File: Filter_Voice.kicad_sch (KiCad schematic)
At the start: 26 parts, among them U3 TL074, U5 SSI2144

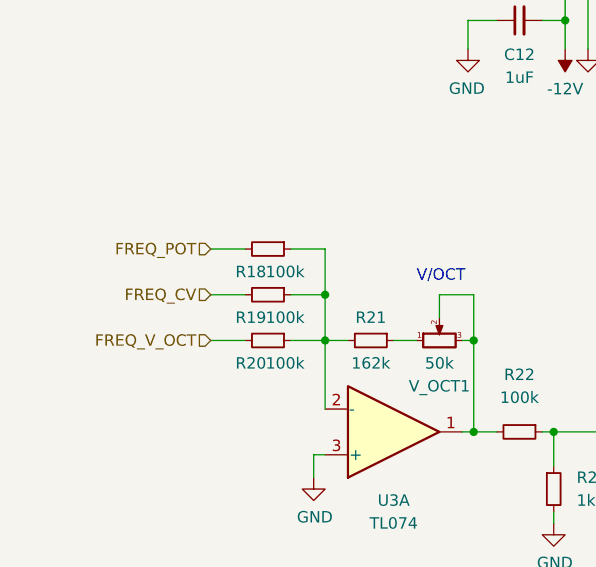
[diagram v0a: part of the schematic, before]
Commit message: Added all voice filter CV; panel draft done
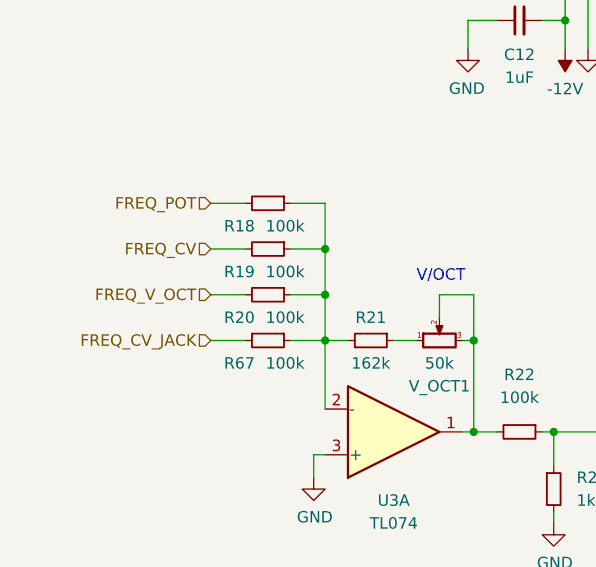
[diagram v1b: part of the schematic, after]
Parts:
- added R67: 100k, Resistor_SMD:R_0603_1608Metric_Pad0.98x0.95mm_HandSolder, symbol Device:R_Small
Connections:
- net at R18.1, R19.1, R20.1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: now also R67.1
- new net FREQ_CV_JACK: R67.2
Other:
- moved on the sheet: R18, R19, R20

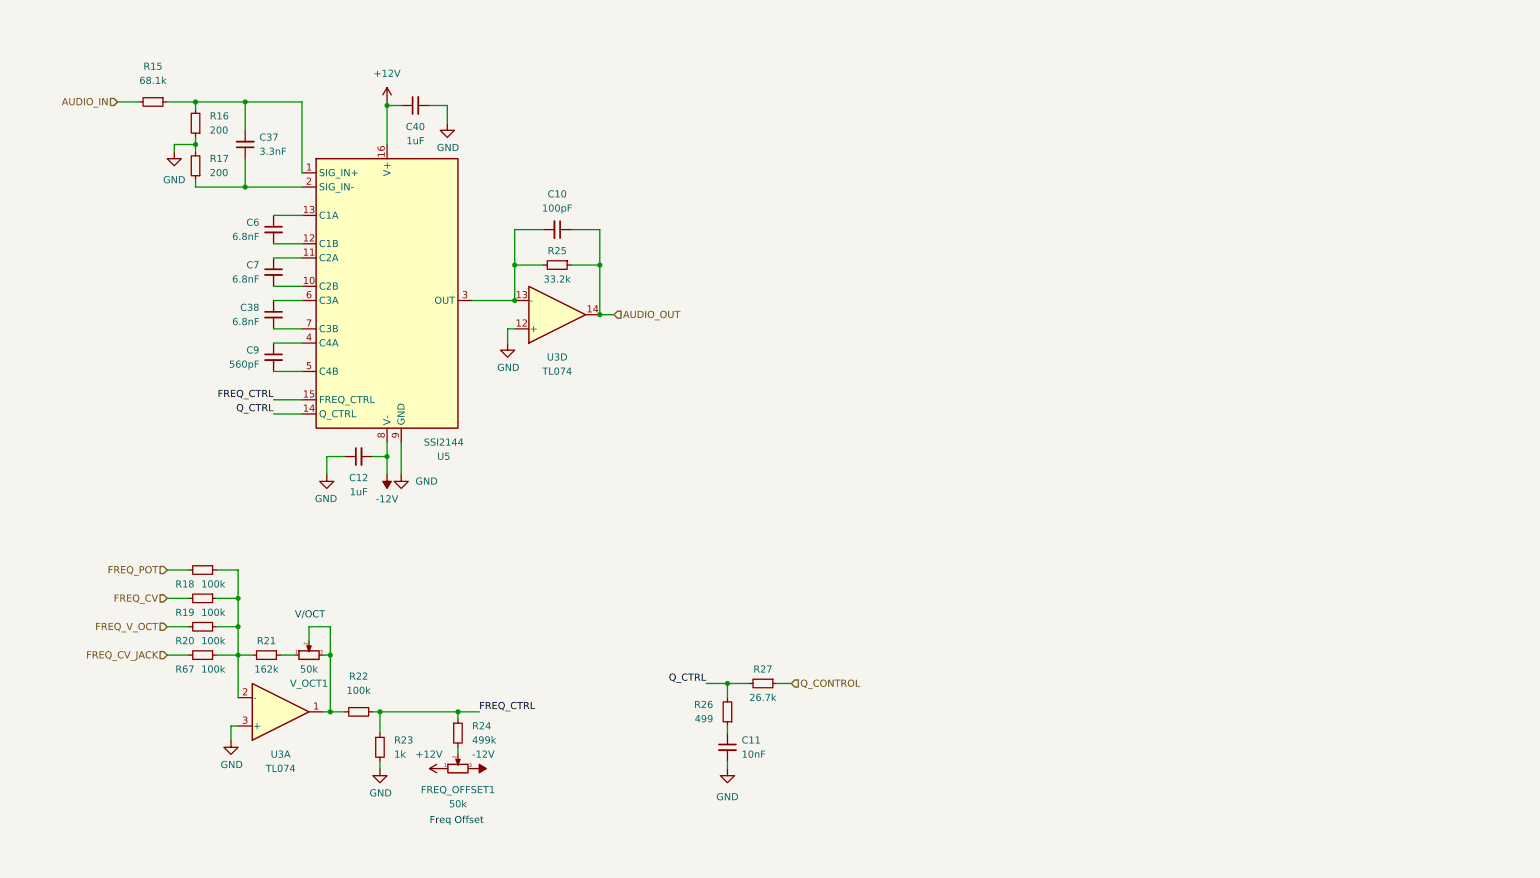
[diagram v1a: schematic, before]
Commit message: Schematic formatting
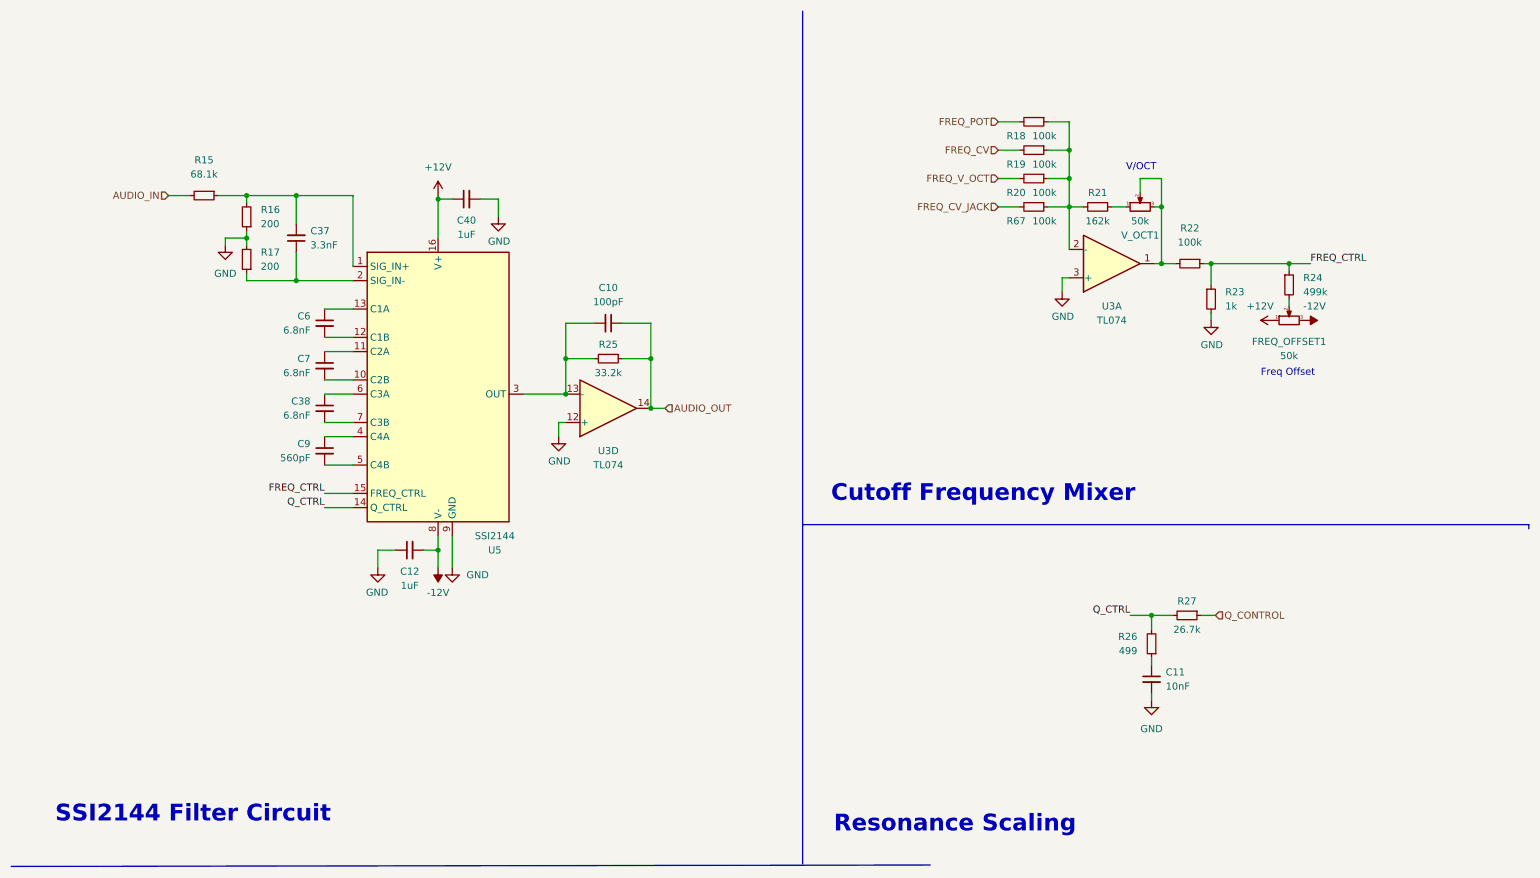
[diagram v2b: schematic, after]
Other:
- note added: "Cutoff Frequency Mixer"
- note added: "Resonance Scaling"
- note added: "SSI2144 Filter Circuit"
- moved on the sheet: C10, C11, C12, C37, C38, C40, C6, C7, C9, FREQ_OFFSET1, R15, R16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

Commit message: Cleaned up panel and PCBs
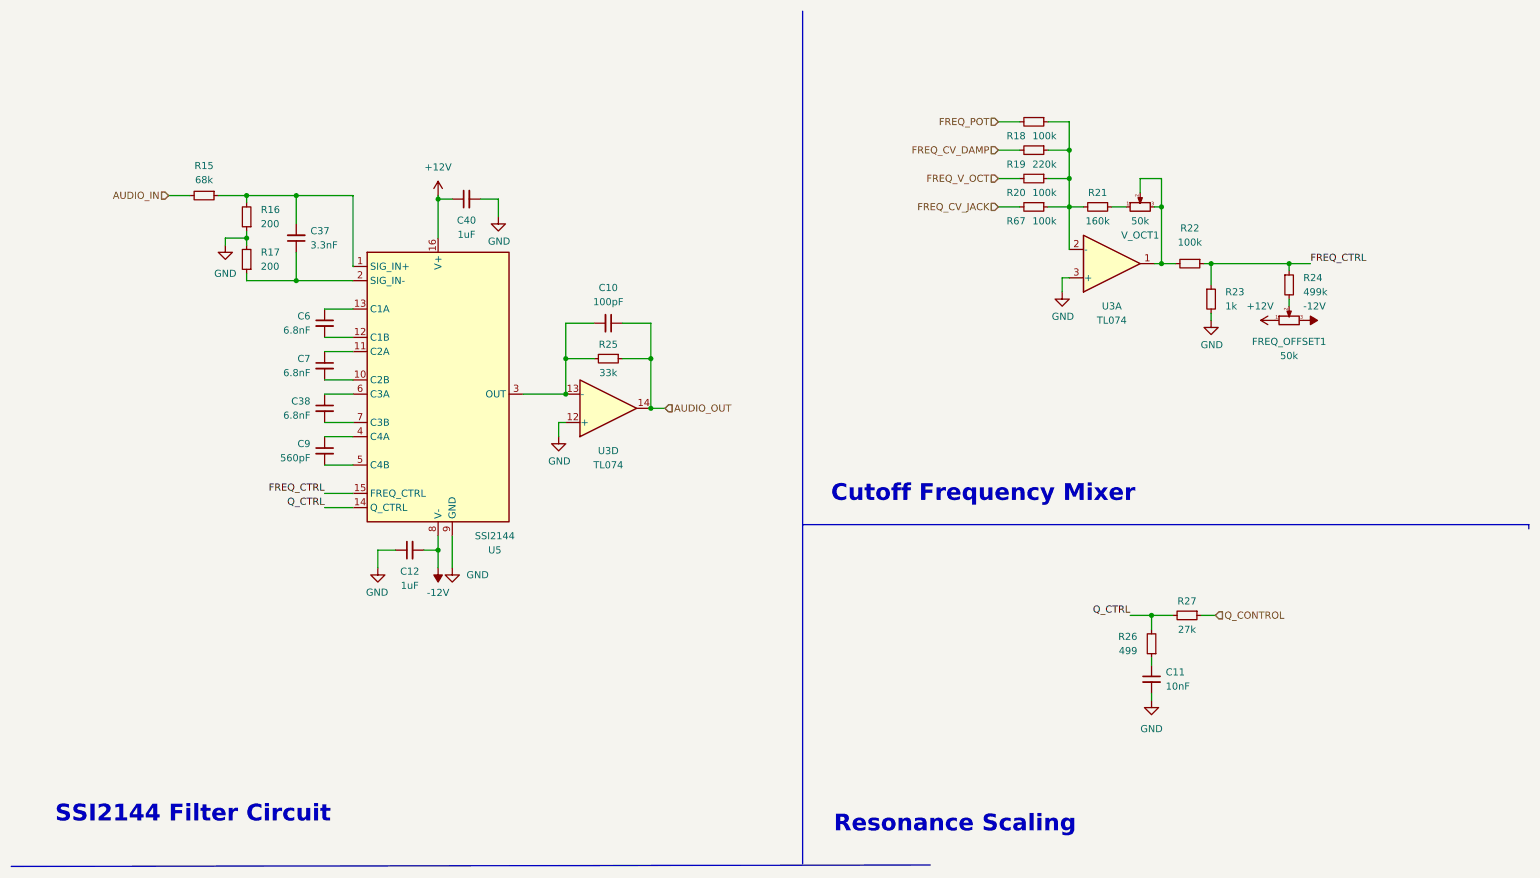
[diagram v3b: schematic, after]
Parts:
- R15: value 68.1k -> 68k
- R19: value 100k -> 220k
- R21: value 162k -> 160k
- R25: value 33.2k -> 33k
- R27: value 26.7k -> 27k
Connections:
- net FREQ_CV renamed FREQ_CV_DAMP
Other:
- note removed: "Freq Offset"
- note removed: "V/OCT"
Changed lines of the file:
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@@
     (effects (font (size 3 3) (thickness 0.6) bold) (justify left bottom))
-  )
-  (text "V/OCT" (at 212.344 41.656 0)
-    (effects (font (size 1.27 1.27)) (justify left bottom))
   )
   (text "SSI2144 Filter Circuit" (at 20.574 158.496 0)
     (effects (font (size 3 3) (thickness 0.6) bold) (justify left bottom))
   )
-  (text "Freq Offset" (at 236.474 78.486 0)
-    (effects (font (size 1.27 1.27)) (justify left bottom))
-  )
   (text "Resonance Scaling" (at 160.02 160.274 0)
     (effects (font (size 3 3) (thickness 0.6) bold) (justify left bottom))
@@
     (effects (font (size 1.27 1.27)) (justify right bottom))
   )
-  (hierarchical_label "FREQ_CV" (shape input) (at 189.484 37.846 180)
+  (hierarchical_label "FREQ_CV_DAMP" (shape input) (at 189.484 37.846 180)
     (effects (font (size 1.27 1.27)) (justify right))
   )
@@
   (symbol (lib_id "Device:R_Small") (at 47.244 45.974 270) (unit 1)
     (in_bom yes) (on_board yes) (fields_autoplaced)
-    (property "Reference" "R15" (id 0) (at 47.244 39.624 90))
-    (property "Value" "68.1k" (id 1) (at 47.244 42.164 90))
+    (property "Reference" "R15" (id 0) (at 47.244 40.64 90))
+    (property "Value" "68k" (id 1) (at 47.244 43.18 90))
     (property "Footprint" "Resistor_SMD:R_0603_1608Metric_Pad0.98x0.95mm_HandSolder" (id 2) (at 47.244 45.974 0)
       (effects (font (size 1.27 1.27)) hide)
@@
     (in_bom yes) (on_board yes)
     (property "Reference" "R21" (id 0) (at 207.264 45.466 90))
-    (property "Value" "162k" (id 1) (at 207.264 50.546 90))
+    (property "Value" "160k" (id 1) (at 207.264 50.546 90))
     (property "Footprint" "Resistor_SMD:R_0603_1608Metric_Pad0.98x0.95mm_HandSolder" (id 2) (at 207.264 48.006 0)
       (effects (font (size 1.27 1.27)) hide)
@@
     (in_bom yes) (on_board yes)
     (property "Reference" "R25" (id 0) (at 119.634 72.644 90))
-    (property "Value" "33.2k" (id 1) (at 119.634 77.724 90))
+    (property "Value" "33k" (id 1) (at 119.634 77.724 90))
     (property "Footprint" "Resistor_SMD:R_0603_1608Metric_Pad0.98x0.95mm_HandSolder" (id 2) (at 119.634 75.184 0)
       (effects (font (size 1.27 1.27)) hide)
@@
     (in_bom yes) (on_board yes)
     (property "Reference" "R27" (id 0) (at 223.266 118.618 90))
-    (property "Value" "26.7k" (id 1) (at 223.266 123.698 90))
+    (property "Value" "27k" (id 1) (at 223.266 123.698 90))
     (property "Footprint" "Resistor_SMD:R_0603_1608Metric_Pad0.98x0.95mm_HandSolder" (id 2) (at 223.266 121.158 0)
       (effects (font (size 1.27 1.27)) hide)
@@
     (in_bom yes) (on_board yes)
     (property "Reference" "R19" (id 0) (at 192.659 40.386 90))
-    (property "Value" "100k" (id 1) (at 197.739 40.386 90))
+    (property "Value" "220k" (id 1) (at 197.739 40.386 90))
     (property "Footprint" "Resistor_SMD:R_0603_1608Metric_Pad0.98x0.95mm_HandSolder" (id 2) (at 195.834 37.846 0)
       (effects (font (size 1.27 1.27)) hide)

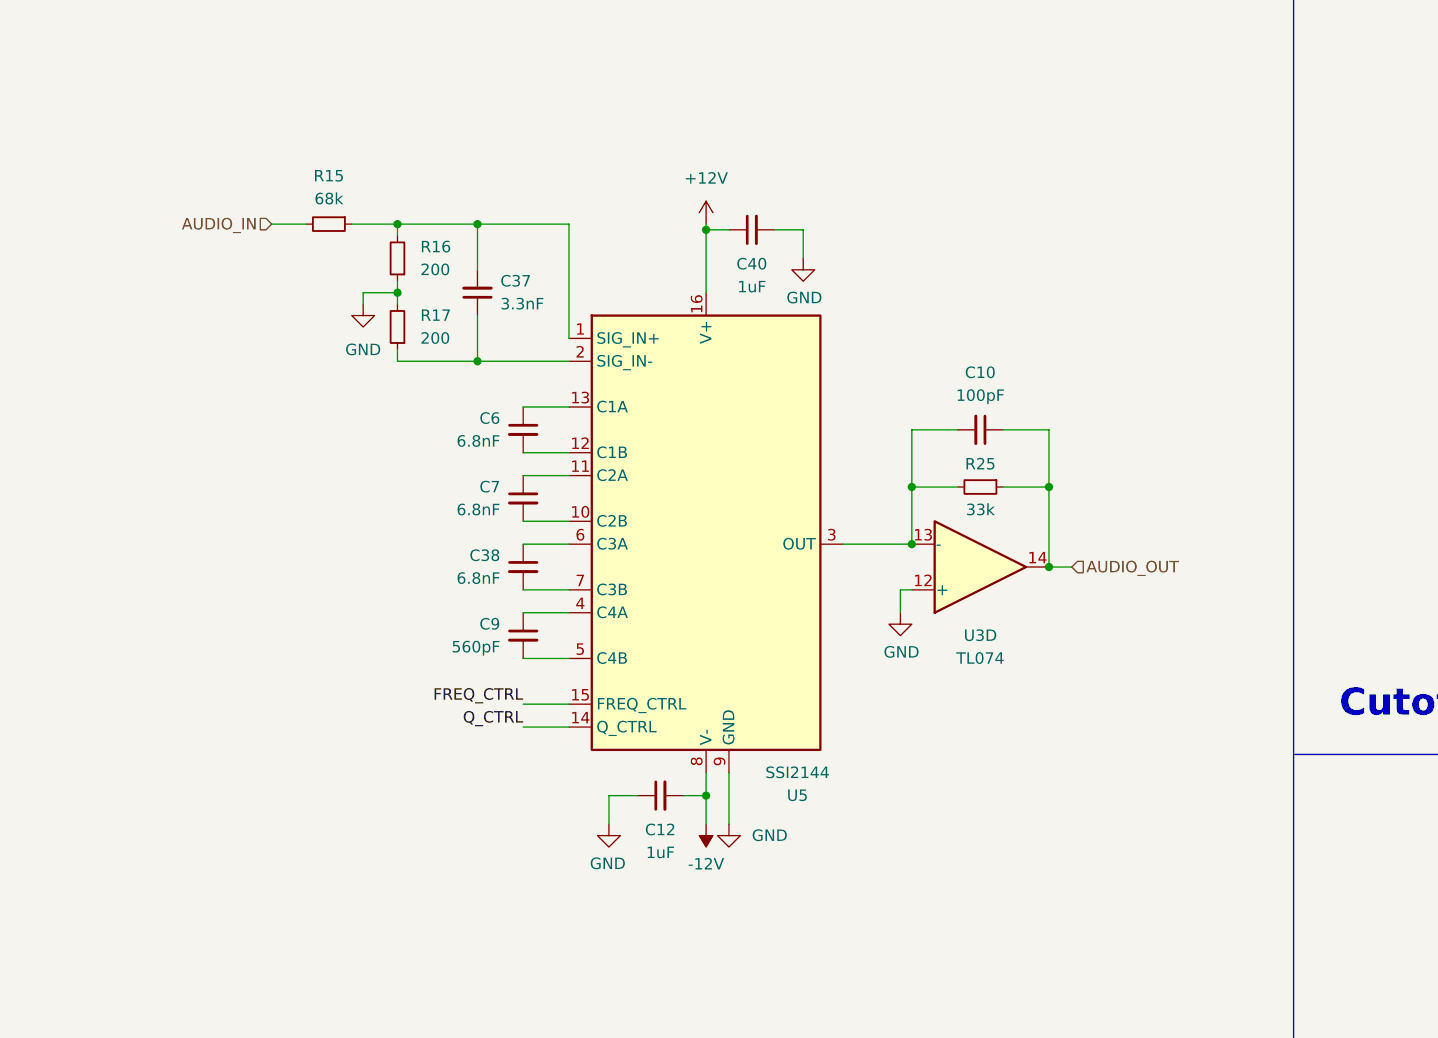
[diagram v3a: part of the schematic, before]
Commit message: Started adding DC blocking caps to audio outputs
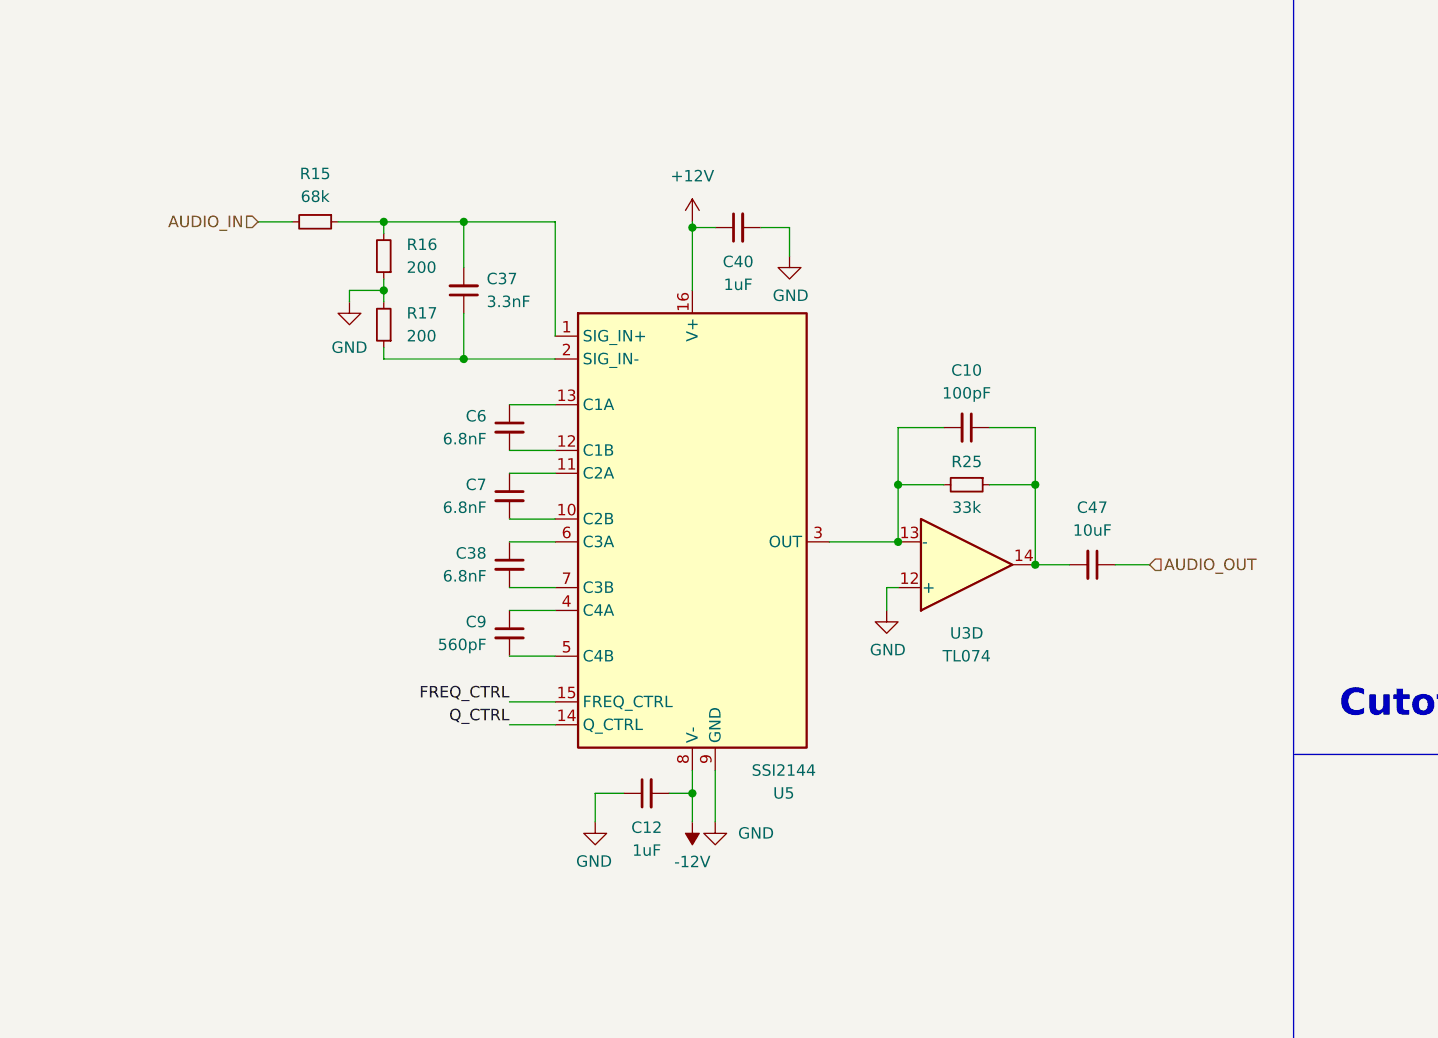
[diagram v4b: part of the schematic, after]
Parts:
- added C47: 10uF, Capacitor_SMD:C_0603_1608Metric_Pad1.08x0.95mm_HandSolder, symbol Device:C_Small
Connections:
- net AUDIO_OUT: now also C47.1; no longer C10.1, R25.1, U3.14
- new net: C10.1, C47.2, R25.1, U3.14
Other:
- moved on the sheet: C10, C12, C37, C38, C40, C6, C7, C9, R15, R16, R17, R25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
